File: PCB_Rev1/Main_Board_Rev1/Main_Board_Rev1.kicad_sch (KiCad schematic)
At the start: 5 parts, among them J1 PRT-14017

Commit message: GND net to M5 holes
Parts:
- H1, H2, H3, H4: footprint MountingHole:MountingHole_5.3mm_M5 -> MountingHole:MountingHole_5.3mm_M5_DIN965_Pad
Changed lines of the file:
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@@
 			)
 		)
-		(property "Footprint" "MountingHole:MountingHole_5.3mm_M5"
+		(property "Footprint" "MountingHole:MountingHole_5.3mm_M5_DIN965_Pad"
 			(at 46.99 171.45 0)
 			(effects
@@
 			)
 		)
-		(property "Footprint" "MountingHole:MountingHole_5.3mm_M5"
+		(property "Footprint" "MountingHole:MountingHole_5.3mm_M5_DIN965_Pad"
 			(at 24.13 171.45 0)
 			(effects
@@
 			)
 		)
-		(property "Footprint" "MountingHole:MountingHole_5.3mm_M5"
+		(property "Footprint" "MountingHole:MountingHole_5.3mm_M5_DIN965_Pad"
 			(at 24.13 180.34 0)
 			(effects
@@
 			)
 		)
-		(property "Footprint" "MountingHole:MountingHole_5.3mm_M5"
+		(property "Footprint" "MountingHole:MountingHole_5.3mm_M5_DIN965_Pad"
 			(at 46.99 180.34 0)
 			(effects

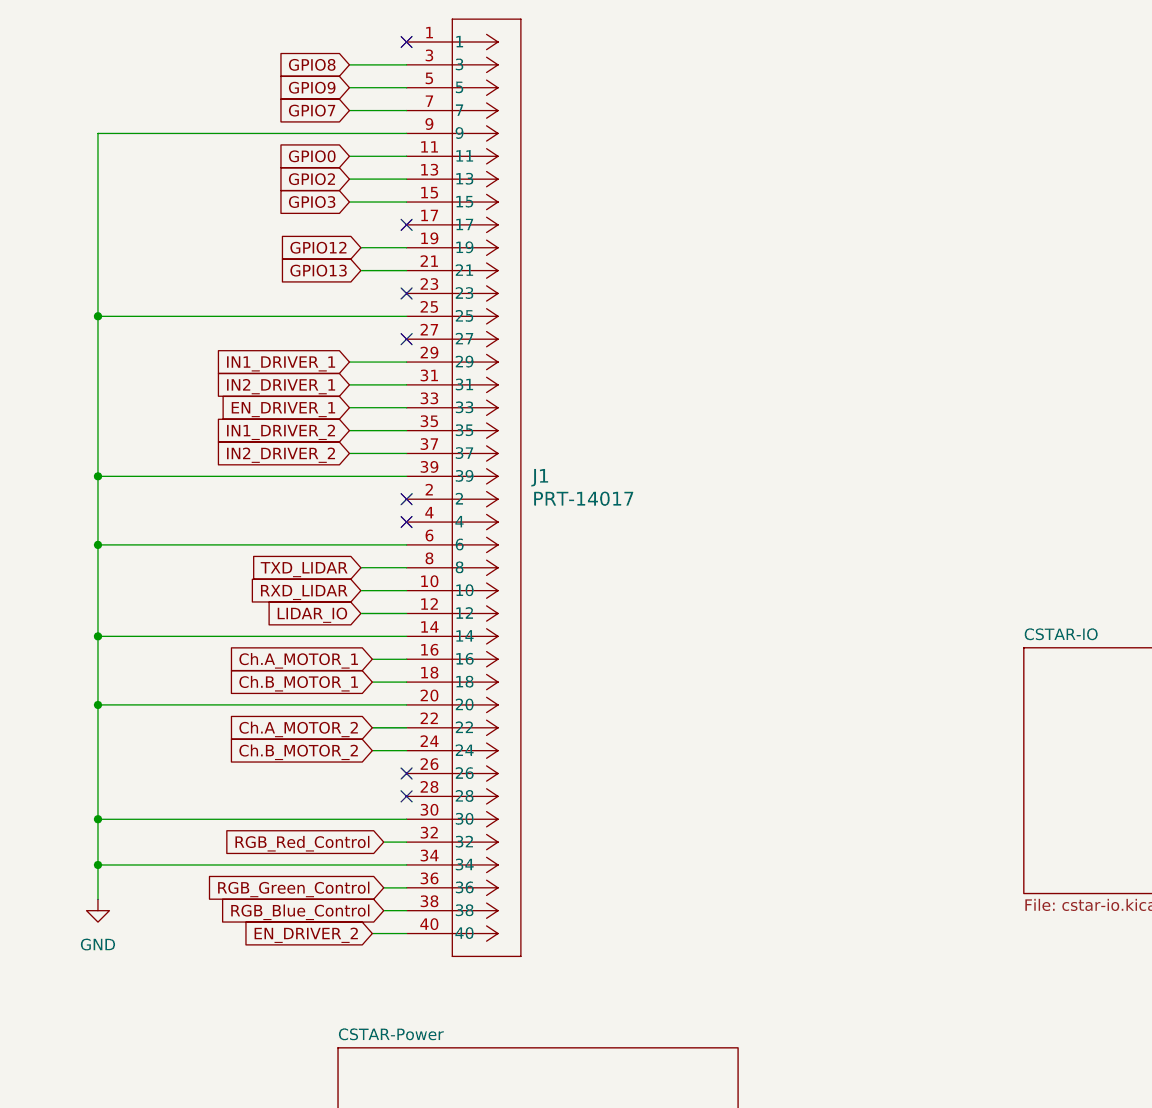
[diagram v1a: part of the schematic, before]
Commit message: Audio Connector Pins
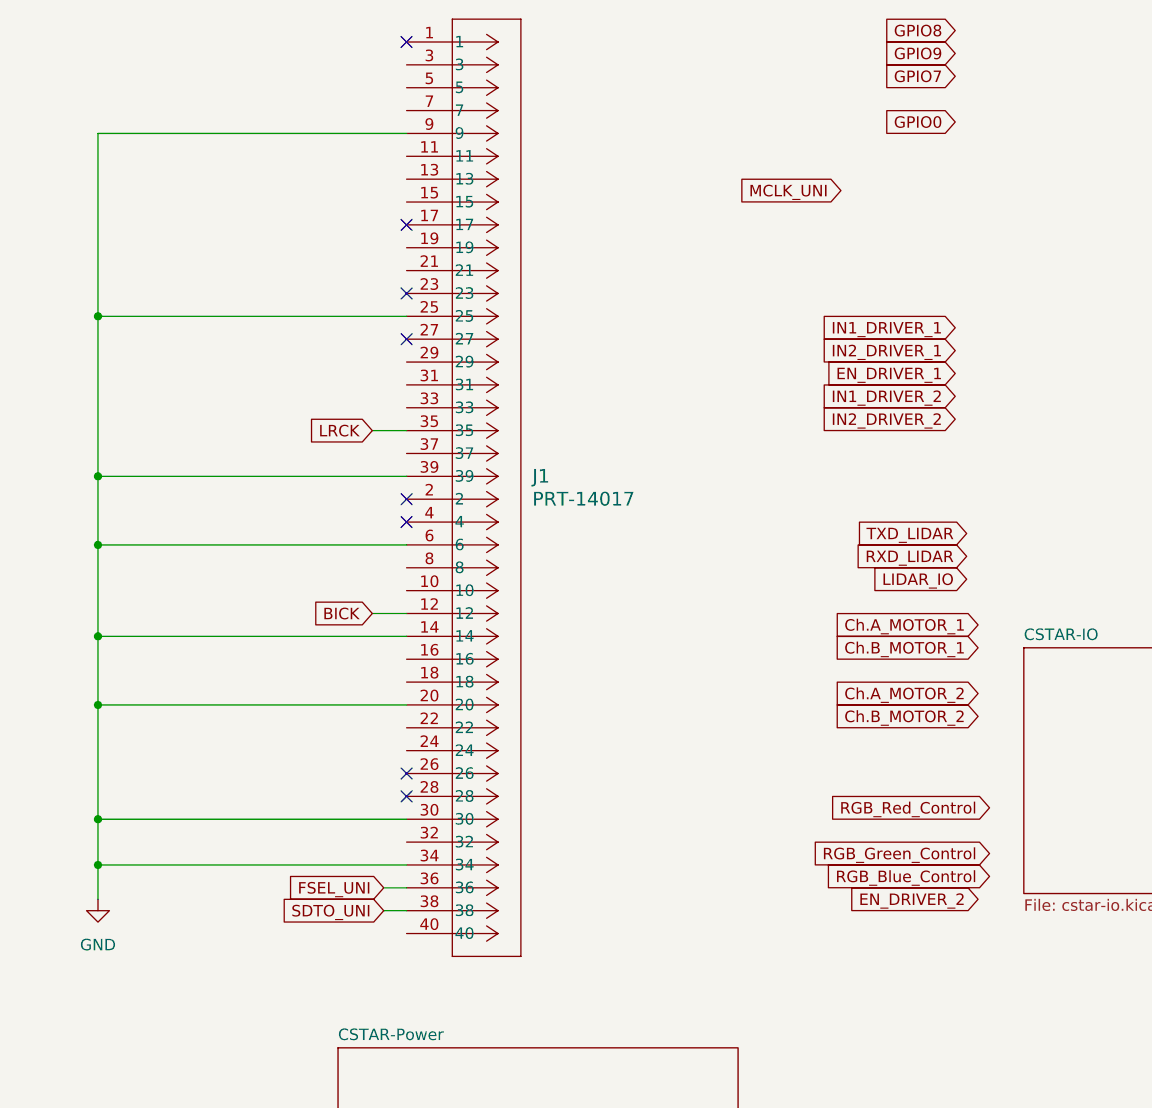
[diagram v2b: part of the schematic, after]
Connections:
- net Ch.A_MOTOR_1: no longer J1.16
- net Ch.A_MOTOR_2: no longer J1.22
- net Ch.B_MOTOR_1: no longer J1.18
- net Ch.B_MOTOR_2: no longer J1.24
- net EN_DRIVER_1: no longer J1.33
- net EN_DRIVER_2: no longer J1.40
- net GPIO0: no longer J1.11
- net GPIO7: no longer J1.7
- net GPIO8: no longer J1.3
- net GPIO9: no longer J1.5
- net IN1_DRIVER_1: no longer J1.29
- net IN1_DRIVER_2: no longer J1.35
- net IN2_DRIVER_1: no longer J1.31
- net IN2_DRIVER_2: no longer J1.37
- net LIDAR_IO: no longer J1.12
- net RGB_Blue_Control: no longer J1.38
- net RGB_Green_Control: no longer J1.36
- net RGB_Red_Control: no longer J1.32
- net RXD_LIDAR: no longer J1.10
- net TXD_LIDAR: no longer J1.8
- net GPIO12: no longer names the net of J1.19
- net GPIO13: no longer names the net of J1.21
- net GPIO2: no longer names the net of J1.13
- net GPIO3: no longer names the net of J1.15
- new net BICK: J1.12
- new net FSEL_UNI: J1.36
- new net LRCK: J1.35
- new net SDTO_UNI: J1.38

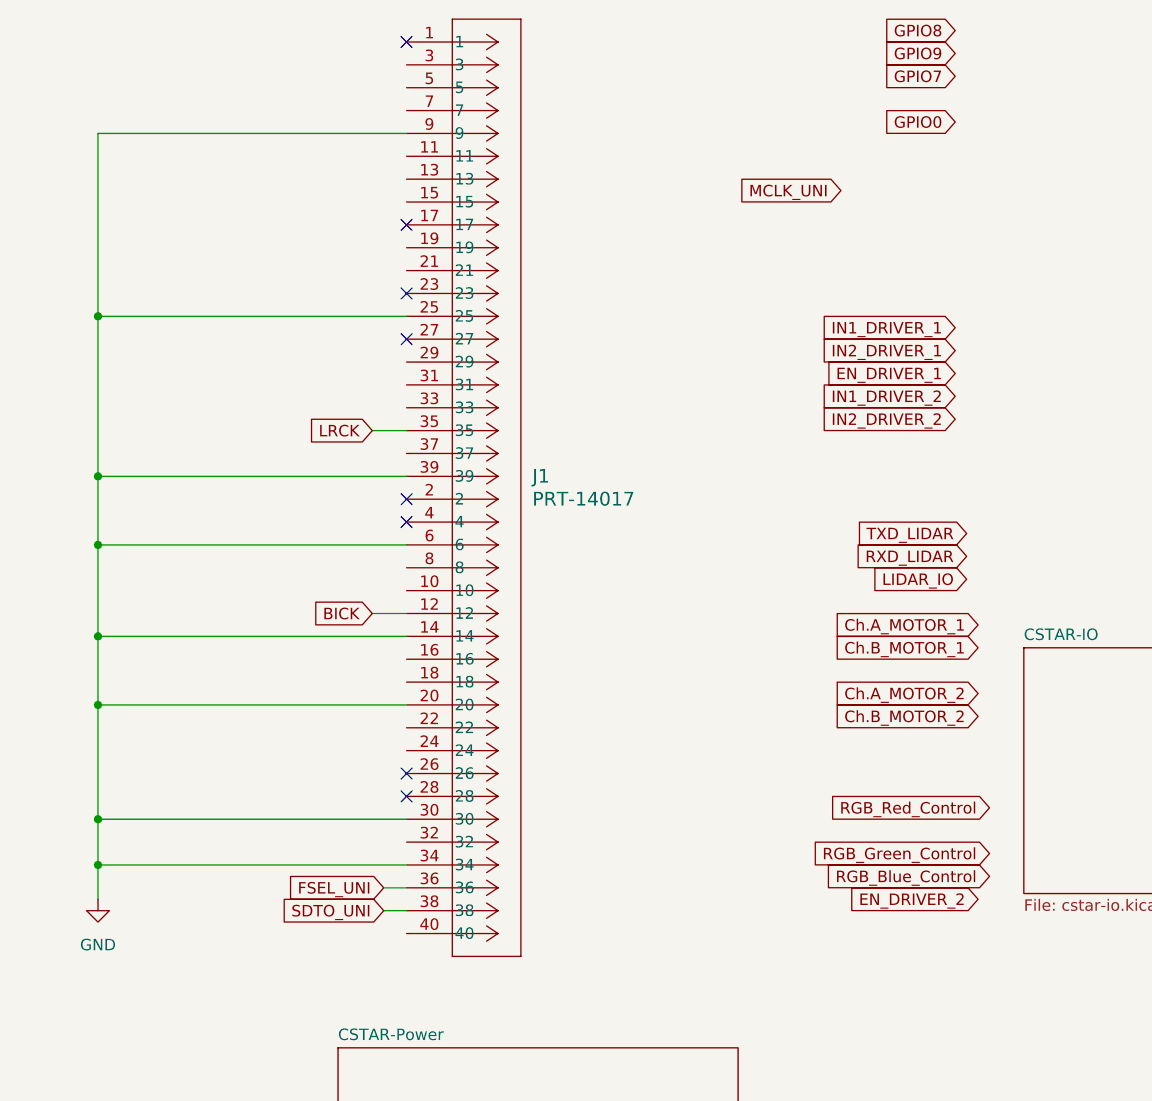
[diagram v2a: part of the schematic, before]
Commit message: Connections Adjustments
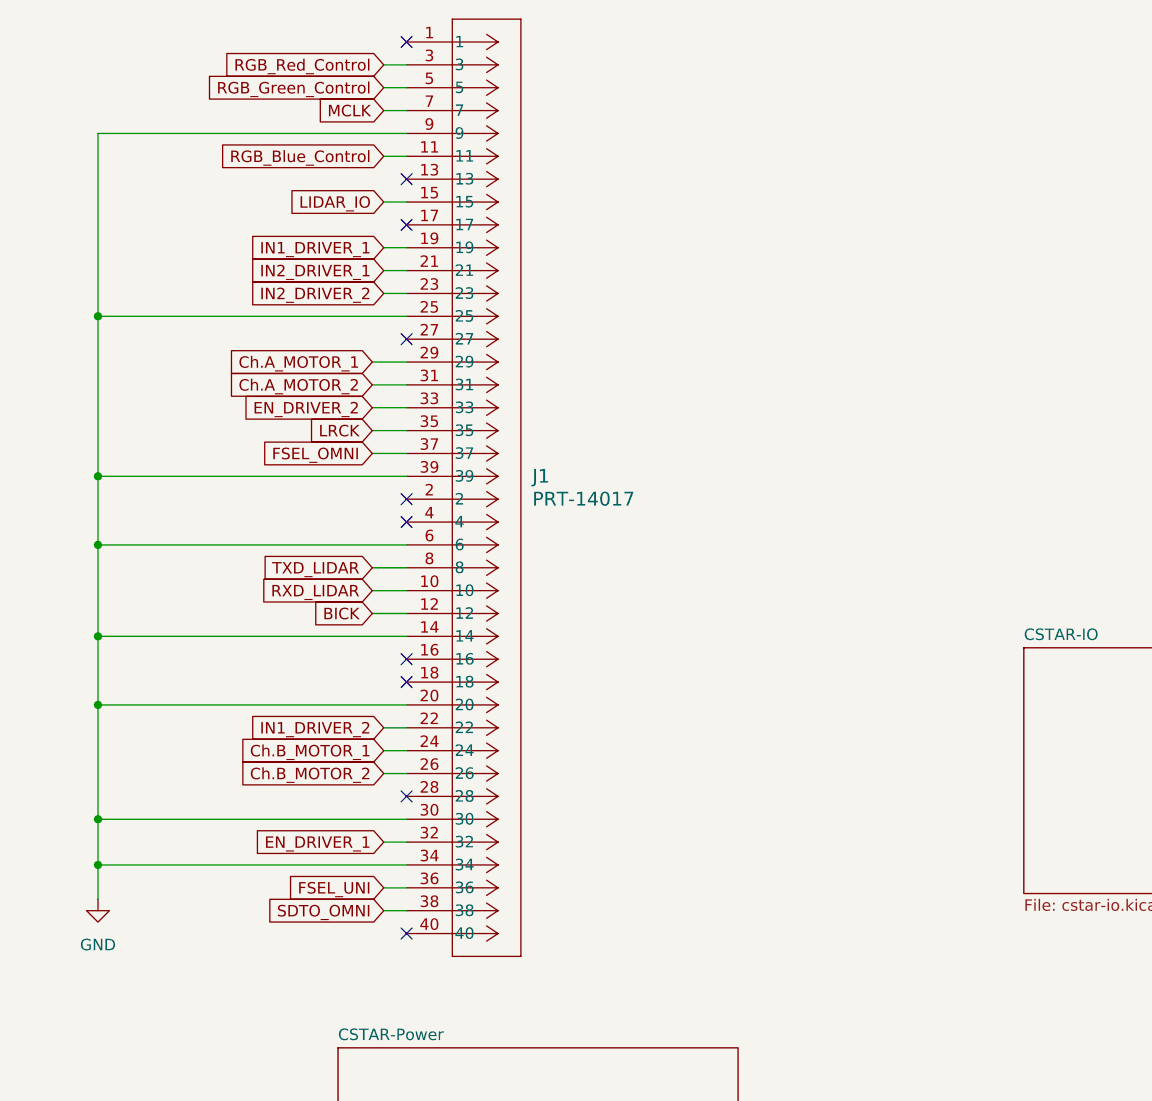
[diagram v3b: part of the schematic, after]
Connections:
- net Ch.A_MOTOR_1: now also J1.29
- net Ch.A_MOTOR_2: now also J1.31
- net Ch.B_MOTOR_1: now also J1.24
- net Ch.B_MOTOR_2: now also J1.26
- net EN_DRIVER_1: now also J1.32
- net EN_DRIVER_2: now also J1.33
- net IN1_DRIVER_1: now also J1.19
- net IN1_DRIVER_2: now also J1.22
- net IN2_DRIVER_1: now also J1.21
- net IN2_DRIVER_2: now also J1.23
- net LIDAR_IO: now also J1.15
- net RGB_Blue_Control: now also J1.11
- net RGB_Green_Control: now also J1.5
- net RGB_Red_Control: now also J1.3
- net RXD_LIDAR: now also J1.10
- net TXD_LIDAR: now also J1.8
- net FSEL_OMNI: now reaches J1.37
- net MCLK: now reaches J1.7
- net SDTO_UNI renamed SDTO_OMNI
- no-connect marks 8 -> 10

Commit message: LCSC + CSV changes
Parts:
- J1: LCSC (none) -> C2859067
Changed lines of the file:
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@@
+			)
+		)
+		(property "LCSC" "C2859067"
+			(at 114.3 17.78 0)
+			(effects
+				(font
+					(size 1.27 1.27)
+				)
+				(hide yes)
 			)
 		)
